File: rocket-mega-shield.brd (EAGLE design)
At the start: 114.3 x 60 mm, 66 parts, among them J1 ExtBatt, J2 Mega R3, J3 XBEE, J4 MICROSD, J5 U.FL, J6 1X6TERMINALBLOCK, Q1 SI7112DN, Q2 BSS138, Q3 BSS138, Q4 SI7112DN, Q5 SI7112DN, Q6 SI7112DN, Q7 SI7112DN, U1 NCP1117DT33G, U2 M74HC4050M, U3 FGPMMOPA6H, U4 BMP180, U5 LSM303DLHCTR, U6 L3GD20TR, U7 ADXL377

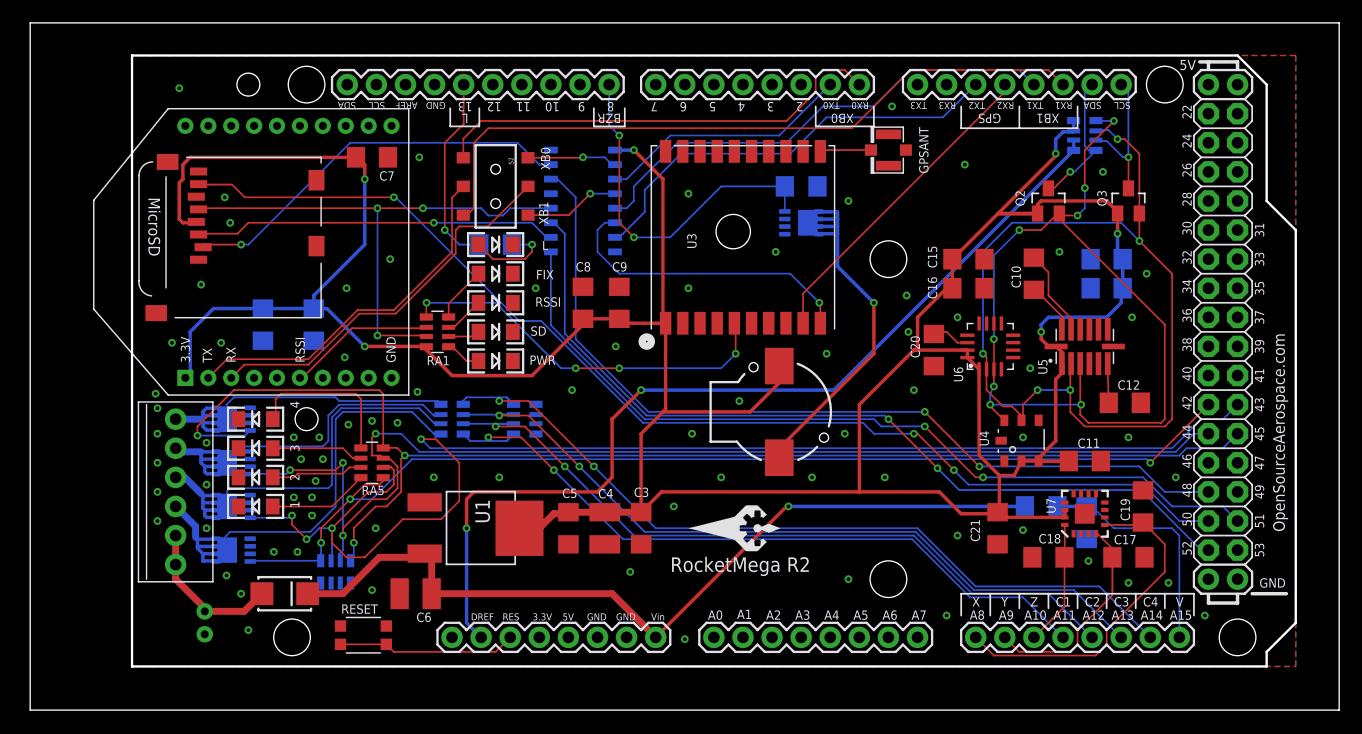
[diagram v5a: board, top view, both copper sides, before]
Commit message: changed out xbee to clean up screen printing lines, trimmed working window down to actual board size
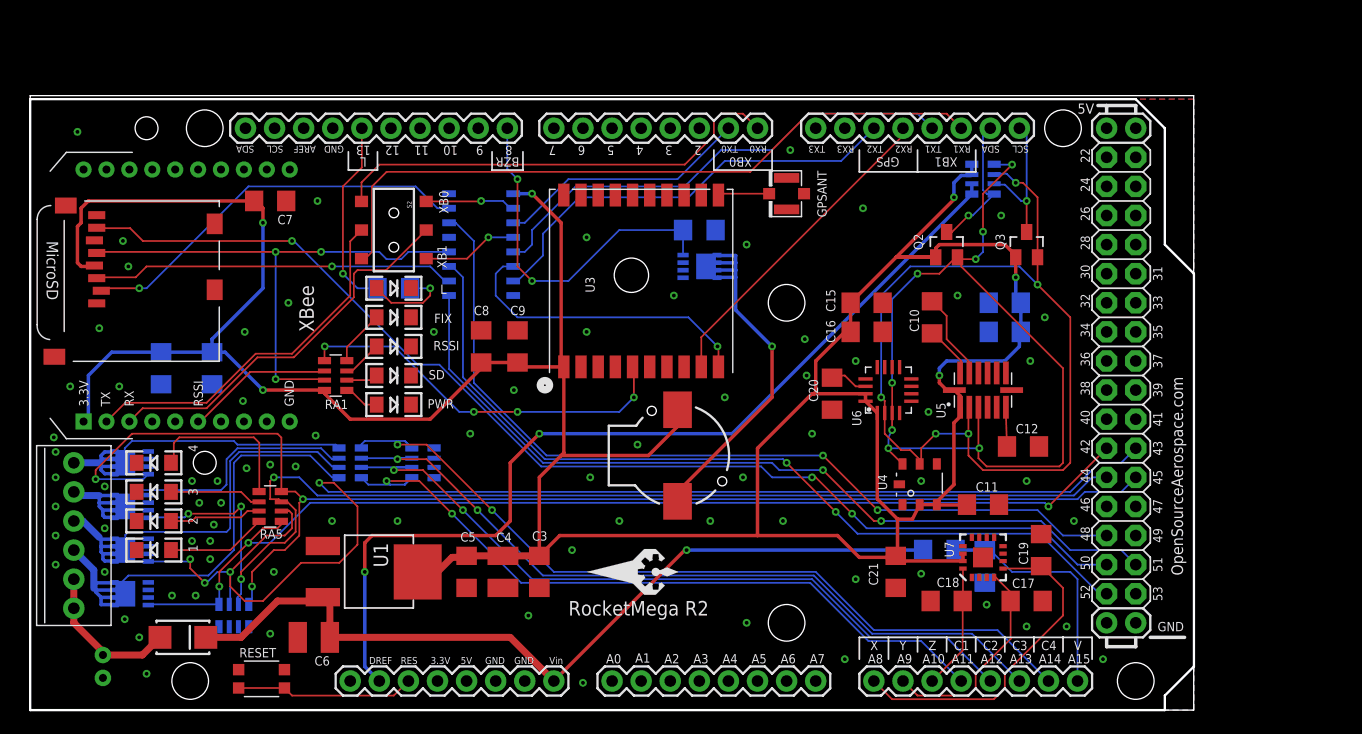
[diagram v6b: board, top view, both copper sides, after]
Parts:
- J3: device adafruit:XBEE -> zortness:XBEE
- moved C1 9.67 mm to (11.4, 29.8)
- moved C10 9.67 mm to (78.7, 34.3)
- moved C11 9.67 mm to (83.2, 17.9)
- moved C12 9.67 mm to (86.7, 23.0)
- moved C17 9.67 mm to (87.0, 9.53)
- moved C18 9.67 mm to (80.0, 9.53)
- moved C19 9.67 mm to (88.3, 14.0)
- moved C2 9.67 mm to (15.9, 29.8)
- moved C20 9.67 mm to (70.0, 27.6)
- moved C21 9.67 mm to (75.6, 12.1)
- moved C3 9.67 mm to (44.5, 12.1)
- moved C4 9.67 mm to (41.3, 12.1)
- moved C5 9.67 mm to (38.1, 12.1)
- moved C6 9.67 mm to (24.8, 6.35)
- moved C8 9.67 mm to (39.4, 31.8)
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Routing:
- net N$3: track 41.9 -> 42.9 mm
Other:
- board size 114.3 x 60 mm -> 101.6 x 53.6 mm
- board text added: "XBee"

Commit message: cleaning up some power nets, flipped buzzer around for better routing
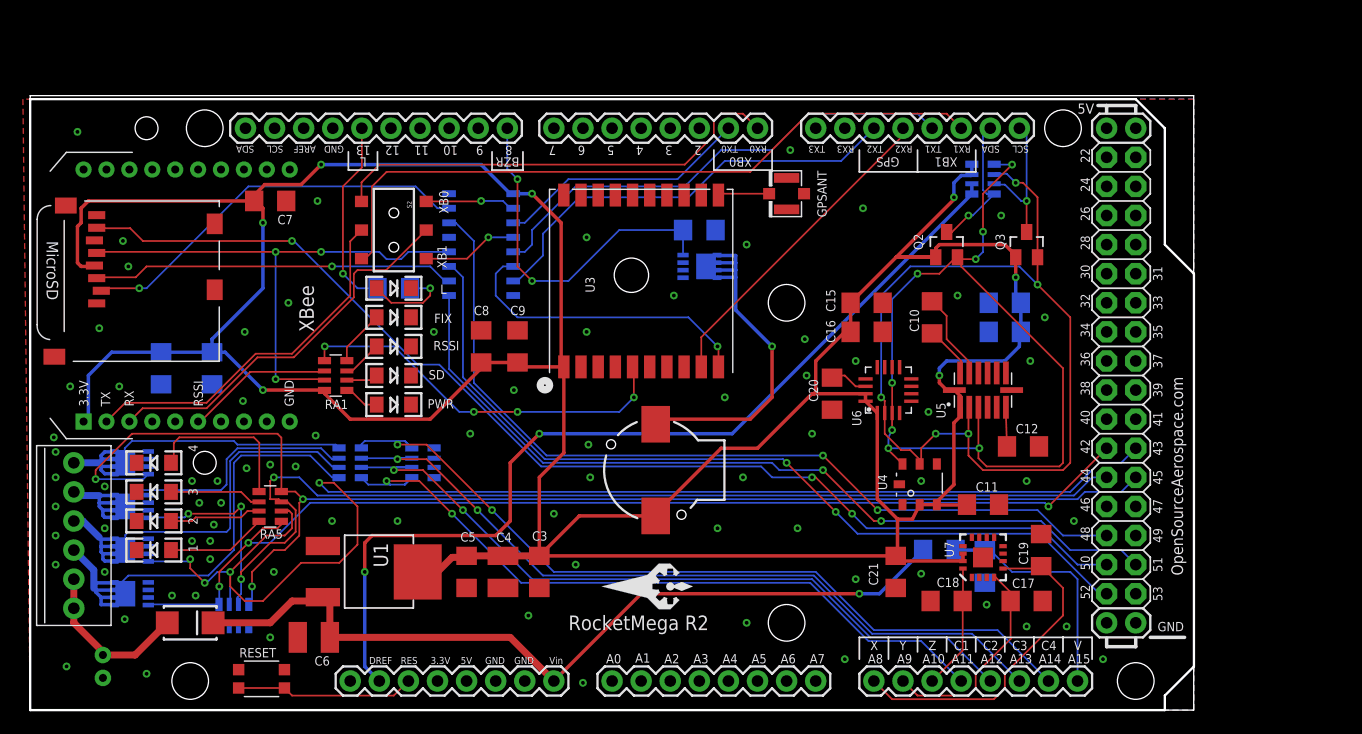
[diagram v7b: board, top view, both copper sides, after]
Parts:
- moved SG1 2.29 mm to (54.6, 21.0), turned to 90 degrees
- moved U$1 1.80 mm to (55.9, 10.8)
- moved D1 1.42 mm to (14.0, 7.62)
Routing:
- net VCC3: track 301.8 -> 327.7 mm, vias 6 -> 7
- net N$13: track 34.7 -> 32.5 mm
- net BATT+: track 13.3 -> 14.5 mm
- net VIN: track 73.5 -> 72.4 mm

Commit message: moving pins around to match the Due pin availablility
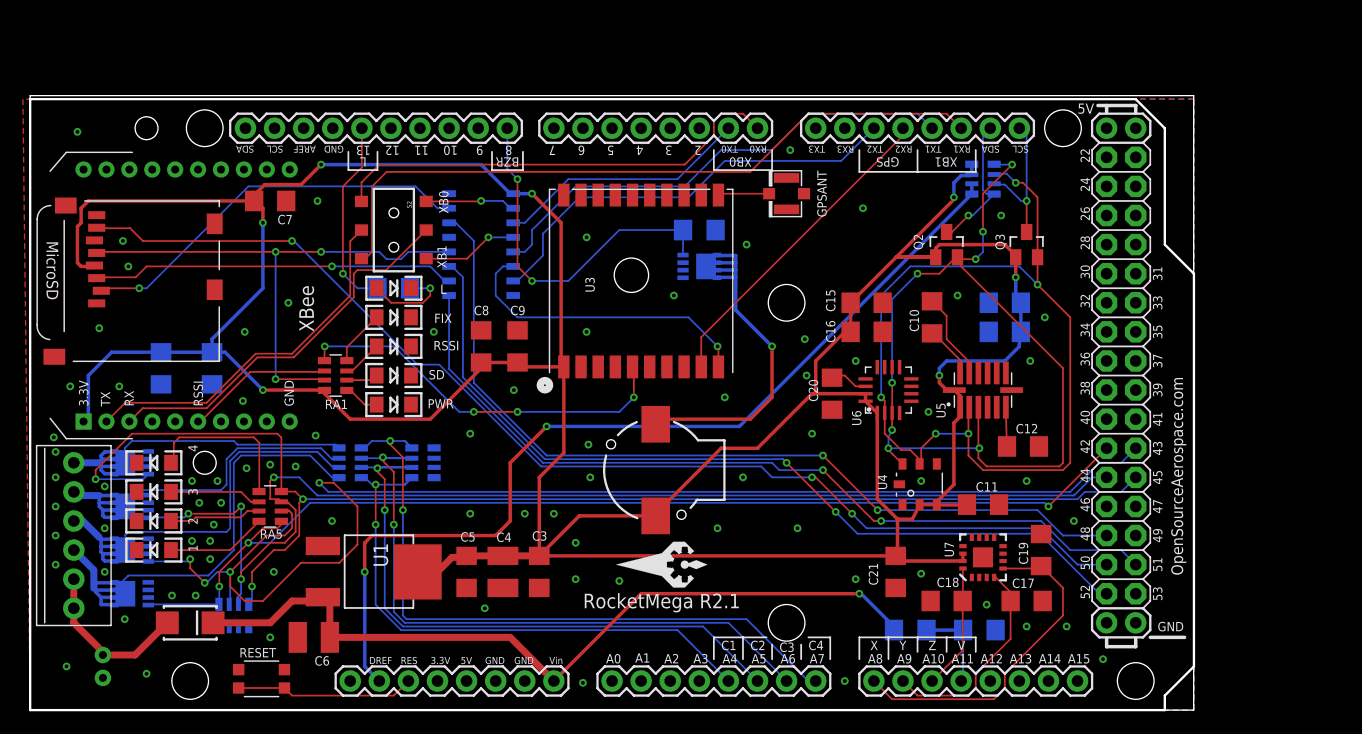
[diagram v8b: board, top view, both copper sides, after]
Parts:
- moved R2 7.43 mm to (76.8, 6.99)
- moved R1 5.58 mm to (82.9, 6.99), turned to 0 degrees
- moved U$1 2.29 mm to (57.1, 12.7)
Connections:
- net MEGAA11: now also R1.2, R2.1; no longer RA3.5, RA4.4
- net MEGAA12: no longer RA3.6, RA4.3
- net MEGAA13: no longer RA3.7, RA4.2
- net MEGAA14: no longer RA3.8, RA4.1
- net MEGAA15: no longer R1.2, R2.1
- net MEGAA4: now also RA3.5, RA4.4
- net MEGAA5: now also RA3.6, RA4.3
- net MEGAA6: now also RA3.7, RA4.2
- net MEGAA7: now also RA3.8, RA4.1
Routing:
- net MEGAA14: track 71.6 -> 0.00 mm, vias 2 -> 0
- net MEGAA13: track 68.0 -> 0.00 mm, vias 2 -> 0
- net MEGAA12: track 65.8 -> 0.00 mm, vias 2 -> 0
- net MEGAA7: track 0.00 -> 59.9 mm, vias 0 -> 2
- net MEGAA6: track 0.00 -> 57.6 mm, vias 0 -> 2
- net MEGAA11: track 63.9 -> 7.70 mm, vias 2 -> 0
- net MEGAA5: track 0.00 -> 55.1 mm, vias 0 -> 2
- net MEGAA4: track 0.00 -> 49.8 mm, vias 0 -> 2
- net MEGAA15: track 20.6 -> 0.00 mm
- net VIN: track 72.4 -> 69.7 mm
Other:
- board text added: "RocketMega R2.1"
- board text removed: "RocketMega R2"
